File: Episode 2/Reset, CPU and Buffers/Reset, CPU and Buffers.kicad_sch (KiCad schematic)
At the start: 0 parts

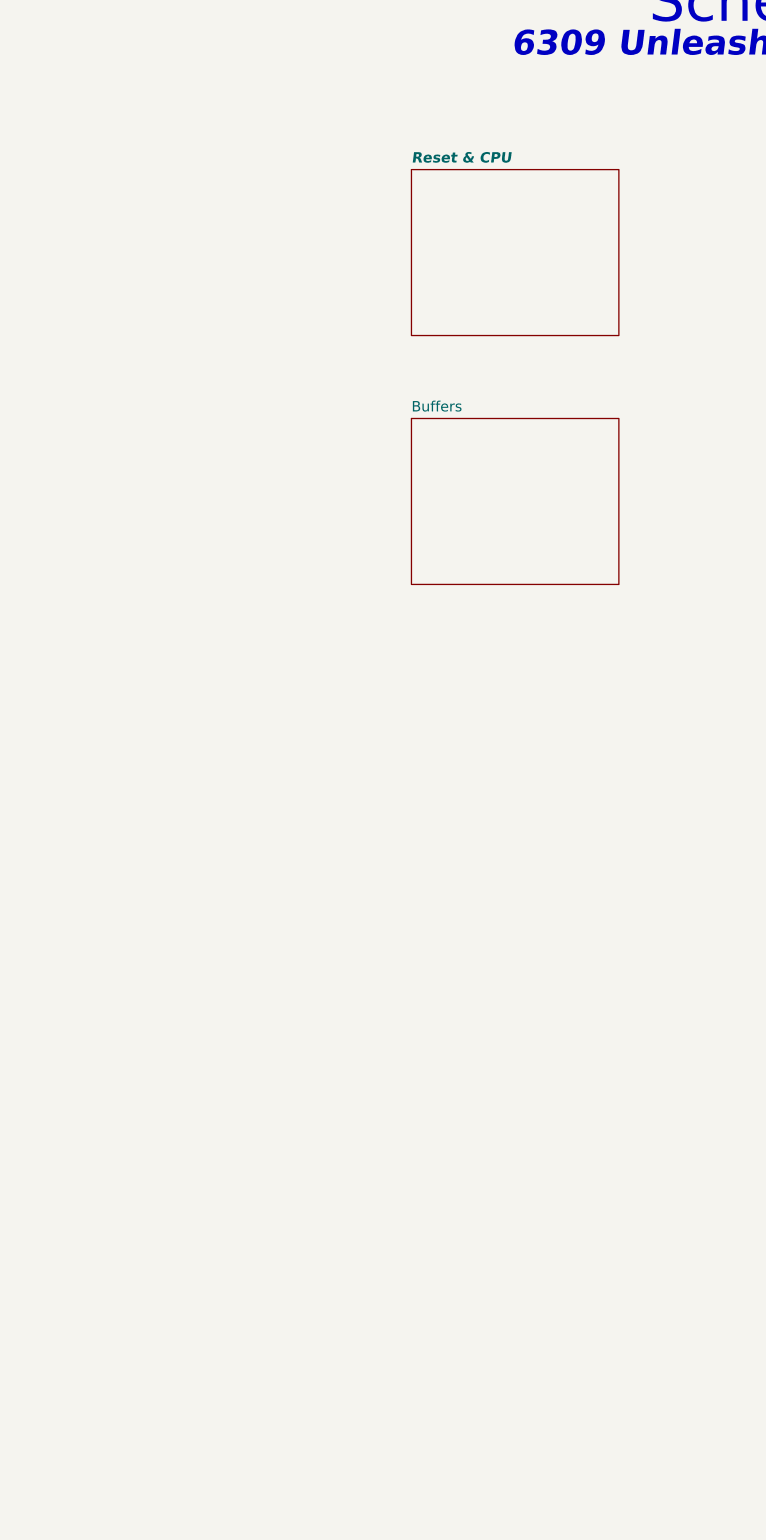
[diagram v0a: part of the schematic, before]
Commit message: Fit both sheets into one
Instead of having one sheet for reset & CPU, and one for bus buffers, I packed everything in one sheet. And it does not look overpacked.
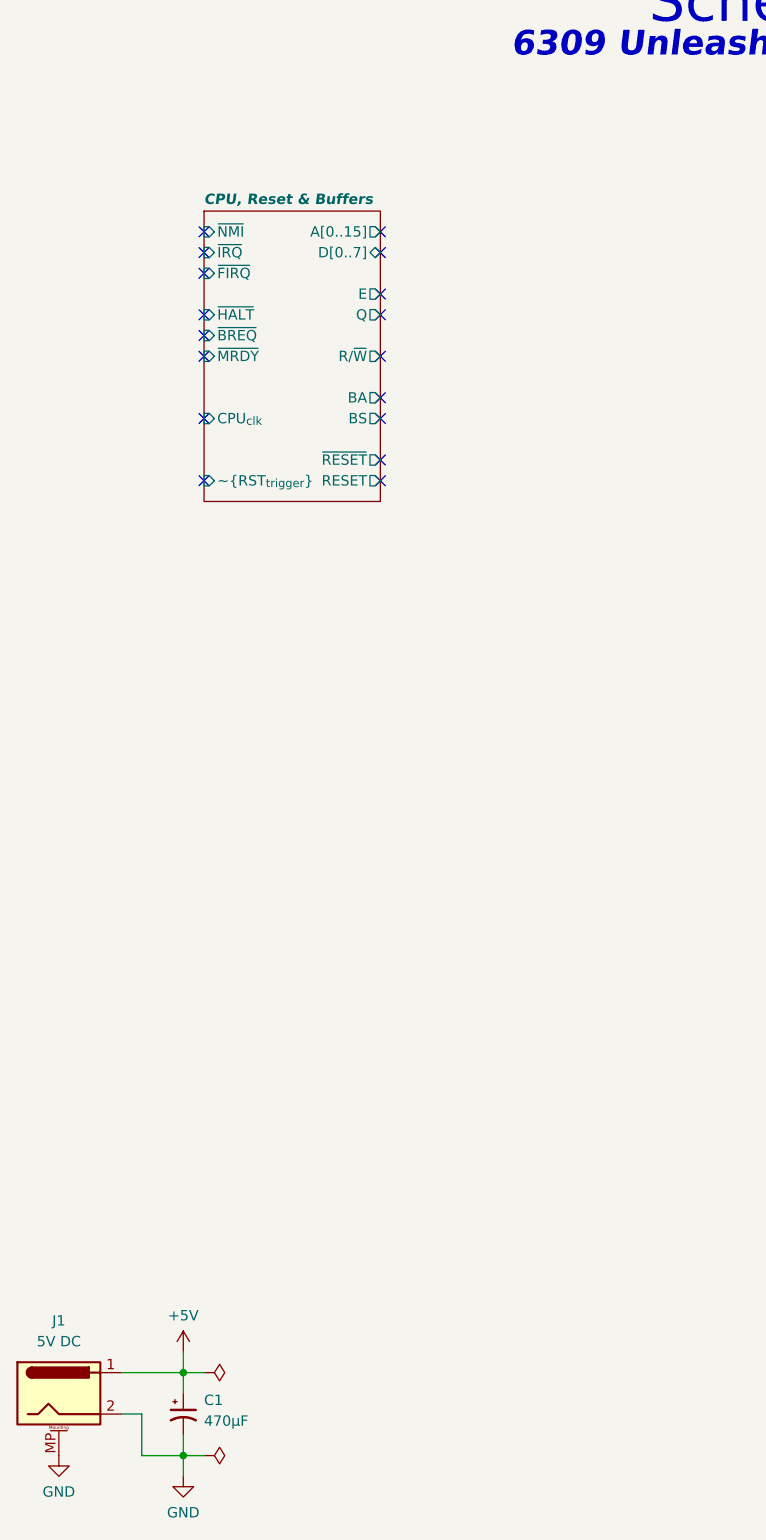
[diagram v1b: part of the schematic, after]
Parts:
- added C1: 470µF, symbol Device:C_Polarized_Small_US
- added J1: 5V DC, symbol Connector:Barrel_Jack_MountingPin
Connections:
- new net +5V: C1.1, J1.1
- new net GND: C1.2, J1.2, J1.MP (MountPin)
- no-connect marks 0 -> 17
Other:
- removed sheet Buffers
- removed sheet Reset & CPU
- added sheet CPU, Reset & Buffers (CPU_RESET_BUFFERS.kicad_sch)
- title: The Clock, The CPU, and Some Buffers -> 6309 Full-Featured Computer

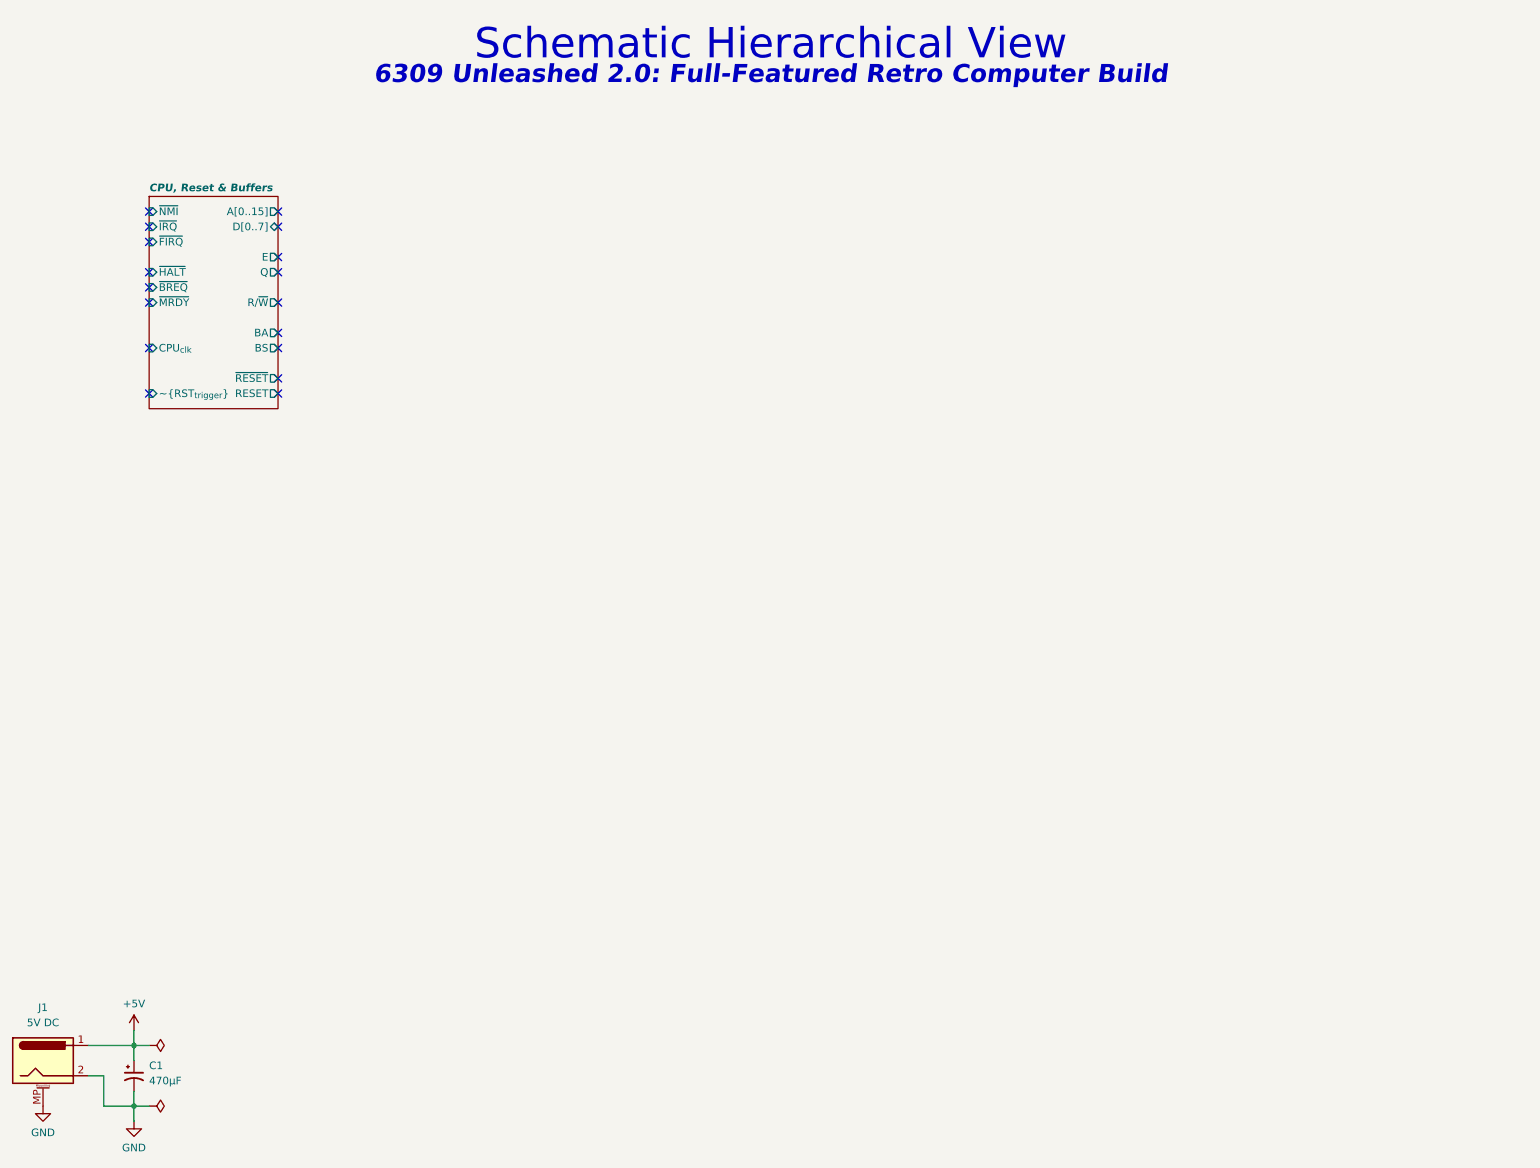
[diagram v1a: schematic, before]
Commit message: Added Arduino Mega to test the circuit. Will be useful for testing the PLDs later
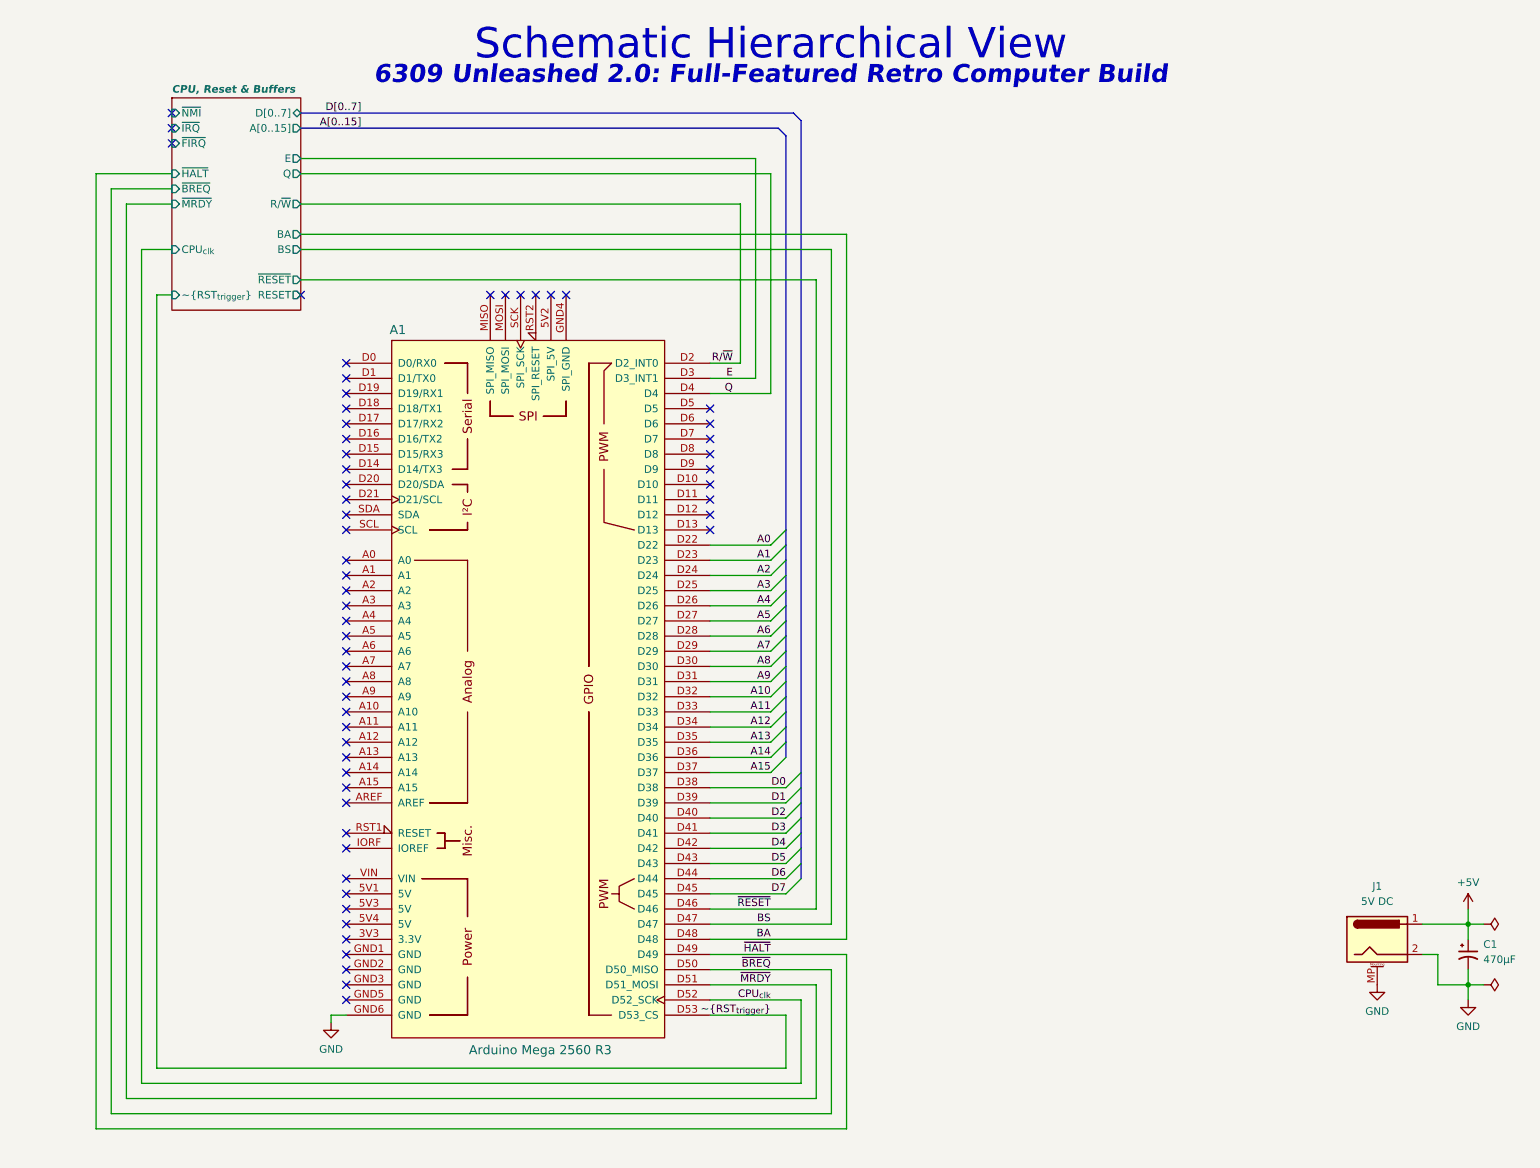
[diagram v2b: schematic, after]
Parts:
- added A1: Arduino Mega 2560 R3, symbol 6309 v2.0:Arduino_Mega2560_R3_Shield
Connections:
- net GND: now also A1.GND6 (GND)
- new net A0: A1.D22
- new net A1: A1.D23
- new net A10: A1.D32
- new net A11: A1.D33
- new net A12: A1.D34
- new net A13: A1.D35
- new net A14: A1.D36
- new net A15: A1.D37
- new net A2: A1.D24
- new net A3: A1.D25
- new net A4: A1.D26
- new net A5: A1.D27
- new net A6: A1.D28
- new net A7: A1.D29
- new net A8: A1.D30
- new net A9: A1.D31
- new net BA: A1.D48
- new net BS: A1.D47
- new net CPU_{clk}: A1.D52 (D52_SCK)
- new net D0: A1.D38
- new net D1: A1.D39
- new net D2: A1.D40
- new net D3: A1.D41
- new net D4: A1.D42
- new net D5: A1.D43
- new net D6: A1.D44
- new net D7: A1.D45
- new net E: A1.D3 (D3_INT1)
- new net Q: A1.D4
- new net R/~{W}: A1.D2 (D2_INT0)
- new net ~{BREQ}: A1.D50 (D50_MISO)
- new net ~{HALT}: A1.D49
- new net ~{MRDY}: A1.D51 (D51_MOSI)
- new net ~{RESET}: A1.D46
- new net ~{RST_{trigger}}: A1.D53 (D53_CS)
- no-connect marks 17 -> 59
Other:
- moved on the sheet: C1, J1

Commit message: Added resistor to MIC1232
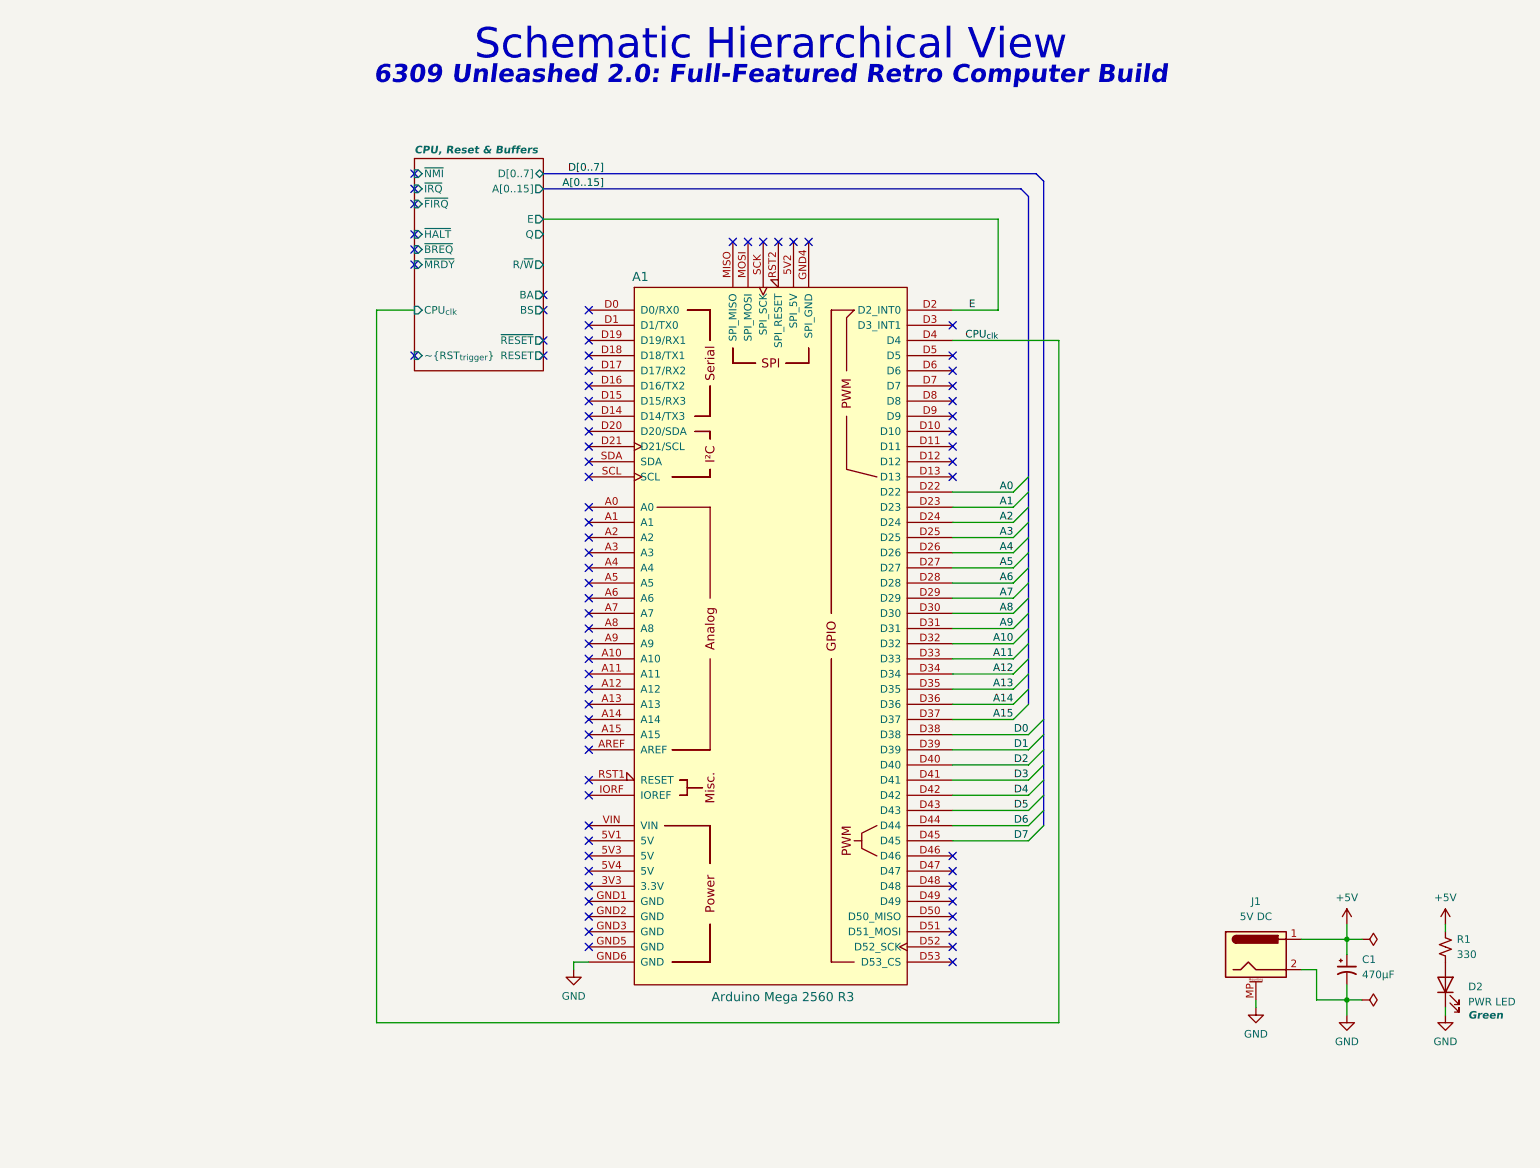
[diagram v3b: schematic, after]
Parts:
- added D2: PWR LED, symbol Device:LED
- added R1: 330, symbol Device:R_Small_US
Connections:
- net Q is gone; now on net CPU_{clk}: A1.D4
- net R/~{W} is gone; now on net E: A1.D2 (D2_INT0)
- net +5V: now also R1.1
- net CPU_{clk}: no longer A1.D52 (D52_SCK)
- net E: no longer A1.D3 (D3_INT1)
- net GND: now also D2.1 (K)
- net BA: no longer names the net of A1.D48
- net BS: no longer names the net of A1.D47
- net ~{BREQ}: no longer names the net of A1.D50 (D50_MISO)
- net ~{HALT}: no longer names the net of A1.D49
- net ~{MRDY}: no longer names the net of A1.D51 (D51_MOSI)
- net ~{RESET}: no longer names the net of A1.D46
- net ~{RST_{trigger}}: no longer names the net of A1.D53 (D53_CS)
- new net: D2.2 (A), R1.2
- no-connect marks 59 -> 75
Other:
- moved on the sheet: A1, C1, J1
